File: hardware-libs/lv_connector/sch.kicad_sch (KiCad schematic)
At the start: 1 part, among them J1 212528-0600

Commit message: Update connector
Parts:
- removed J1: 212528-0600, 212528-0600:212528-06YY_1, symbol 212528-0600:212528-0600
- added J1: 76825-0006, 768250006, symbol 76825-0006:76825-0006
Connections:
- net +24V: now also J1.4
- net GND: now also J1.5
- net can+: now also J1.1
- net can-: now also J1.2
- new net shield: J1.3
- no-connect marks 0 -> 2

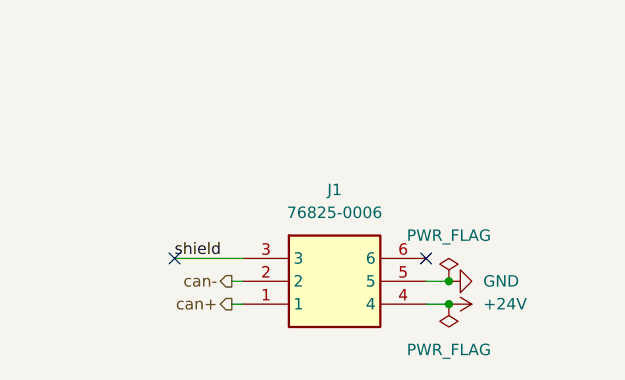
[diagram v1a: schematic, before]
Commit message: Update hardware libs to remove anotations + ticked some todos
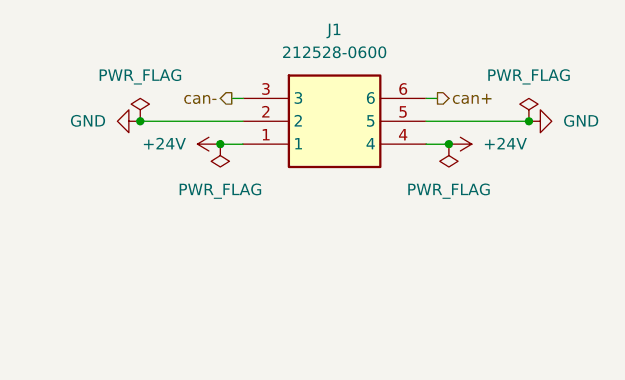
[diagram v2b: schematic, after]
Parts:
- removed J1: 76825-0006, 768250006, symbol 76825-0006:76825-0006
- added J1: 212528-0600, 212528-06YY_1, symbol 212528-0600:212528-0600
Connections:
- net +24V: now also J1.1, J1.4
- net GND: now also J1.2, J1.5
- net can+: now also J1.6
- net can-: now also J1.3
- no-connect marks 2 -> 0
